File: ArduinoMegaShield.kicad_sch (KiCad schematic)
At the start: 23 parts, among them J1 Power, J10 Conn_01x04_Socket, J11 Conn_01x04_Socket, J2 PWM, J3 Analog, J4 PWM, J5 Analog, J6 Communication, J7 Digital, J8 Conn_01x04_Socket, J9 Conn_01x04_Socket, Q1 IRLB8721PBF, Q2 IRLB8721PBF, U1 MP6500_Pololu, U2 MP6500_Pololu

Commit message: Finished Schematic
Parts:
- removed J10, J11: Conn_01x04_Socket, symbol Connector:Conn_01x04_Socket
- removed R2, R3, R5, R6: 20R, symbol Device:R_US
- added J11, J12, J13, J14: Conn_01x02_Socket, Connector_PinSocket_2.54mm:PinSocket_1x02_P2.54mm_Vertical, symbol Connector:Conn_01x02_Socket
- added J15, J16: Conn_01x04, Connector_JST:JST_EH_S4B-EH_1x04_P2.50mm_Horizontal, symbol Connector_Generic:Conn_01x04
- added J17: Conn_01x10_Socket, Connector_PinSocket_2.54mm:PinSocket_1x10_P2.54mm_Vertical, symbol Connector:Conn_01x10_Socket
- added J18: Barrel_Jack_Switch, Connector_BarrelJack:BarrelJack_CUI_PJ-102AH_Horizontal, symbol Connector:Barrel_Jack_Switch
- added J9: Conn_01x04_Socket, Connector_PinSocket_2.54mm:PinSocket_1x04_P2.54mm_Vertical, symbol Connector:Conn_01x04_Socket
- added Q3, Q4, Q5, Q6, Q7: IRLB8721PBF, Package_TO_SOT_THT:TO-220-3_Vertical, symbol Transistor_FET:IRLB8721PBF
- added R2, R3, R5, R6, R7: 10K, Resistor_SMD:R_0805_2012Metric_Pad1.20x1.40mm_HandSolder, symbol Device:R
- C1, C2: footprint (none) -> Capacitor_THT:CP_Radial_D6.3mm_P2.50mm
- J10: renamed from J9; footprint (none) -> Connector_PinSocket_2.54mm:PinSocket_1x04_P2.54mm_Vertical
- J8: footprint (none) -> Connector_PinSocket_2.54mm:PinSocket_1x04_P2.54mm_Vertical
- R1, R4: footprint (none) -> Resistor_SMD:R_0805_2012Metric_Pad1.20x1.40mm_HandSolder
- U1, U2: footprint (none) -> Module:Pololu_Breakout-16_15.2x20.3mm
- renumbered J3 to J2, J5 to J3, J7 to J4, J2 to J5, J4 to J6, J6 to J7
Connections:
- net *10: now also Q7.1 (G), R7.1
- net *11: now also Q1.1 (G), R1.1
- net *12: now also Q2.1 (G), R2.1
- net *6: now also Q3.1 (G), R3.1
- net *7: now also R4.1, Q4.1 (G)
- net *8: now also Q5.1 (G), R5.1
- net *9: now also Q6.1 (G), R6.1
- net +12V: now also U1.16 (VMOT), U2.16 (VMOT), J11.1 (Pin_1), J11.2 (Pin_2), J13.1 (Pin_1), J13.2 (Pin_2), J17.1 (Pin_1), J17.3 (Pin_3), J17.5 (Pin_5), J17.7 (Pin_7), J17.9 (Pin_9), J18.1; no longer U1.9 (VMOT), U2.9 (VMOT)
- net GND: now also U1.15 (GND), U1.9 (GND), U2.15 (GND), U2.9 (GND), J18.2, J9.2 (Pin_2), Q3.3 (S), Q4.3 (S), Q5.3 (S), Q6.3 (S), Q7.3 (S), R2.2, R3.2, R5.2, R6.2, R7.2; no longer U1.10 (GND), U1.16 (GND), U2.10 (GND), U2.16 (GND)
- net SCL/21: now also J9.3 (Pin_3)
- net SDA/20: now also J9.4 (Pin_4)
- net VCC: now also J9.1 (Pin_1)
- net at U1.11 (A2): now also J15.4 (Pin_4)
- net at U1.12 (A1): now also J15.3 (Pin_3)
- net at U1.13 (B1): now also J15.2 (Pin_2)
- net at U1.14 (B2): now also J15.1 (Pin_1)
- net at Q1.2 (D): now also J12.1 (Pin_1), J12.2 (Pin_2)
- net at U2.11 (A2): now also J16.4 (Pin_4)
- net at U2.12 (A1): now also J16.3 (Pin_3)
- net at U2.13 (B1): now also J16.2 (Pin_2)
- net at U2.14 (B2): now also J16.1 (Pin_1)
- net at Q2.2 (D): now also J14.1 (Pin_1), J14.2 (Pin_2)
- new net: J17.10 (Pin_10), Q7.2 (D)
- new net: J17.2 (Pin_2), Q3.2 (D)
- new net: J17.4 (Pin_4), Q4.2 (D)
- new net: J17.6 (Pin_6), Q5.2 (D)
- new net: J17.8 (Pin_8), Q6.2 (D)
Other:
- note added: "Heating Capacitors (zigzag Resistors)"
- note added: "Heating Capacitors between"
- note added: "J15 and J16 CONNECTORS STILL UNDECIDED"
- note added: "Power Supply"
- note added: "Valve MOSFETs"
- title: (none) -> Arduino Mega Shield Schematic (Sylveon)
- moved on the sheet: J10, Q1, R1

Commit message: Update
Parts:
- J15, J16: footprint Connector_JST:JST_EH_S4B-EH_1x04_P2.50mm_Horizontal -> Connector_JST:JST_XH_B4B-XH-A_1x04_P2.50mm_Vertical
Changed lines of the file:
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@@
 			)
 		)
-		(property "Footprint" "Connector_JST:JST_EH_S4B-EH_1x04_P2.50mm_Horizontal"
+		(property "Footprint" "Connector_JST:JST_XH_B4B-XH-A_1x04_P2.50mm_Vertical"
 			(at 154.94 39.37 0)
 			(effects
@@
 			)
 		)
-		(property "Footprint" "Connector_JST:JST_EH_S4B-EH_1x04_P2.50mm_Horizontal"
+		(property "Footprint" "Connector_JST:JST_XH_B4B-XH-A_1x04_P2.50mm_Vertical"
 			(at 218.44 39.37 0)
 			(effects

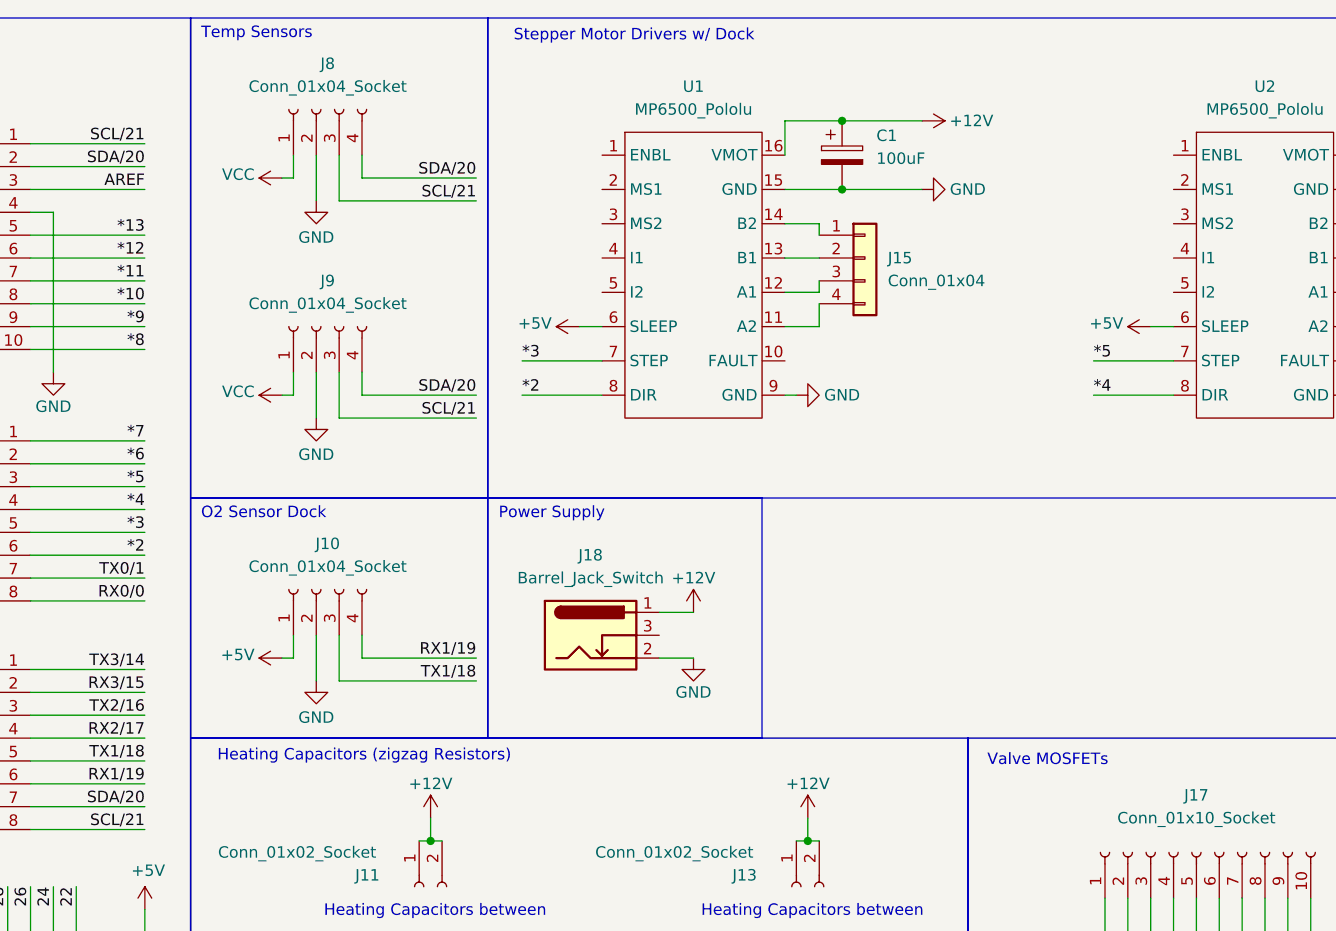
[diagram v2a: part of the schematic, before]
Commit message: Layout Placement done
-no fuse yet
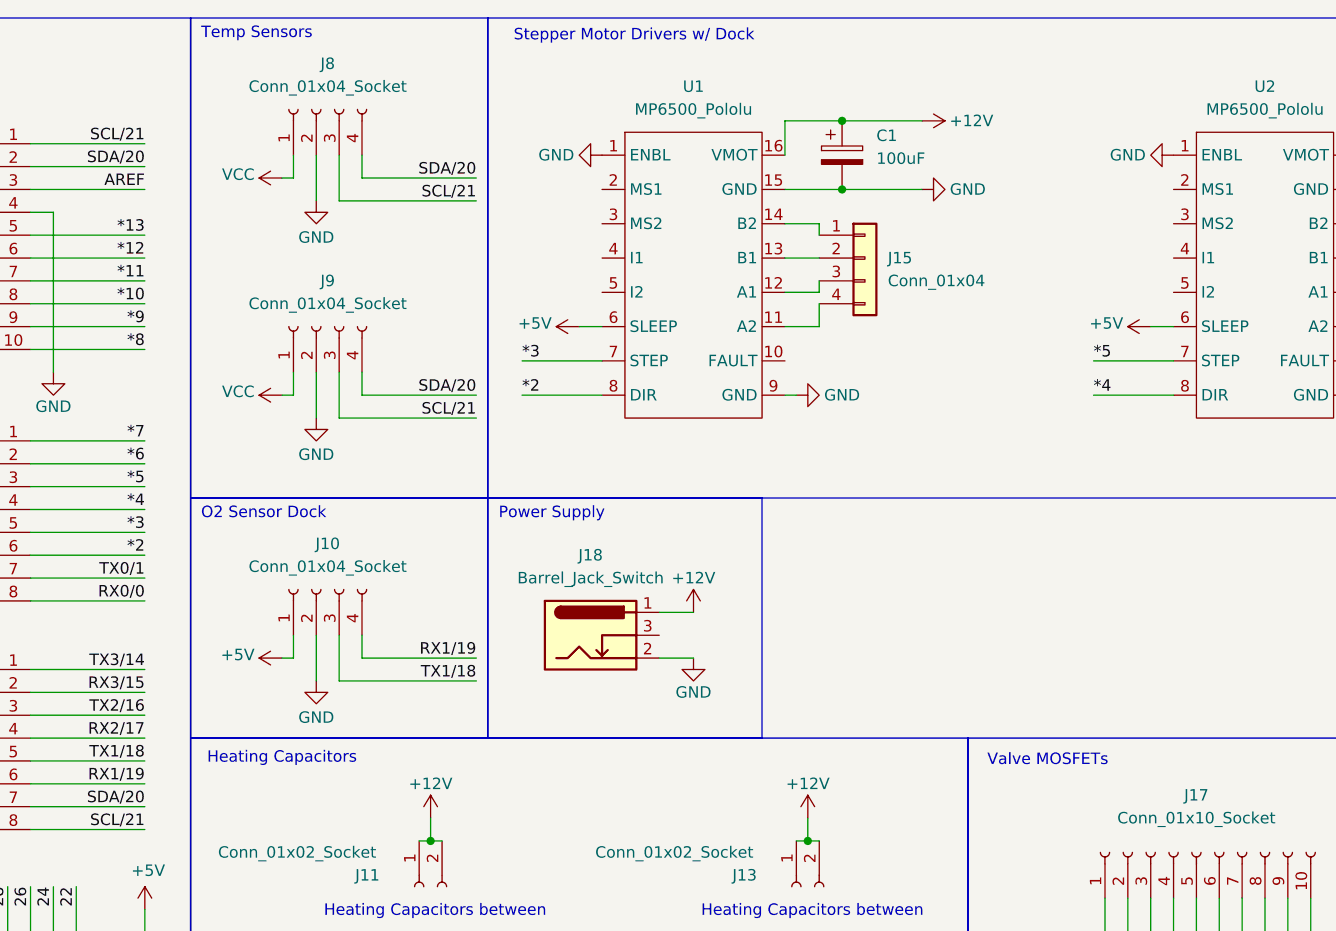
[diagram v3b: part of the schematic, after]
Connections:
- net GND: now also U1.1 (ENBL), U2.1 (ENBL)
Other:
- note added: "Heating Capacitors"
- note removed: "Heating Capacitors (zigzag Resistors)"
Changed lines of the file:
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@@
 		)
 	)
-	(text "Heating Capacitors (zigzag Resistors)"
+	(text "Heating Capacitors"
 		(exclude_from_sim no)
-		(at 99.314 94.742 0)
+		(at 90.17 94.996 0)
 		(effects
 			(font
@@
 	(symbol
 		(lib_id "power:GND")
+		(at 189.23 27.94 270)
+		(unit 1)
+		(exclude_from_sim no)
+		(in_bom yes)
+		(on_board yes)
+		(dnp no)
+		(property "Reference" "#PWR042"
+			(at 182.88 27.94 0)
+			(effects
+				(font
+					(size 1.27 1.27)
+				)
+				(hide yes)
+			)
+		)
+		(property "Value" "GND"
+			(at 184.15 27.94 90)
+			(effects
+				(font
+					(size 1.27 1.27)
+				)
+			)
+		)
+		(property "Footprint" ""
+			(at 189.23 27.94 0)
+			(effects
+				(font
+					(size 1.27 1.27)
+				)
+			)
+		)
+		(property "Datasheet" ""
+			(at 189.23 27.94 0)
+			(effects
+				(font
+					(size 1.27 1.27)
+				)
+			)
+		)
+		(property "Description" ""
+			(at 189.23 27.94 0)
+			(effects
+				(font
+					(size 1.27 1.27)
+				)
+				(hide yes)
+			)
+		)
+		(pin "1"
+		)
+		(instances
+			(project "ArduinoMegaShield"
+				(path "/e63e39d7-6ac0-4ffd-8aa3-1841a4541b55"
+					(reference "#PWR042")
+					(unit 1)
+				)
+			)
+		)
+	)
+	(symbol
+		(lib_id "power:GND")
 		(at 175.26 139.7 0)
 		(unit 1)
@@
 					(unit 1)
 				)
+			)
+		)
+	)
+	(symbol
+		(lib_id "power:GND")
+		(at 125.73 27.94 270)
+		(unit 1)
+		(exclude_from_sim no)
+		(in_bom yes)
+		(on_board yes)
+		(dnp no)
+		(property "Reference" "#PWR041"
+			(at 119.38 27.94 0)
+			(effects
+				(font
+					(size 1.27 1.27)
+				)
+				(hide yes)
+			)
+		)
+		(property "Value" "GND"
+			(at 120.65 27.94 90)
+			(effects
+				(font
+					(size 1.27 1.27)
+				)
+			)
+		)
+		(property "Footprint" ""
+			(at 125.73 27.94 0)
+			(effects
+				(font
+					(size 1.27 1.27)
+				)
+			)
+		)
+		(property "Datasheet" ""
+			(at 125.73 27.94 0)
+			(effects
+				(font
+					(size 1.27 1.27)
+				)
+			)
+		)
+		(property "Description" ""
+			(at 125.73 27.94 0)
+			(effects
+				(font
+					(size 1.27 1.27)
+				)
+				(hide yes)
+			)
+		)
+		(pin "1"
+		)
+		(instances
+			(project "ArduinoMegaShield"
+				(path "/e63e39d7-6ac0-4ffd-8aa3-1841a4541b55"
+					(reference "#PWR041")
+					(unit 1)
+				)

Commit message: Final Layout
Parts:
- removed J11, J12, J13, J14: Conn_01x02_Socket, Connector_PinSocket_2.54mm:PinSocket_1x02_P2.54mm_Vertical, symbol Connector:Conn_01x02_Socket
- removed J17: Conn_01x10_Socket, Connector_PinSocket_2.54mm:PinSocket_1x10_P2.54mm_Vertical, symbol Connector:Conn_01x10_Socket
- removed J18: Barrel_Jack_Switch, Connector_BarrelJack:BarrelJack_CUI_PJ-102AH_Horizontal, symbol Connector:Barrel_Jack_Switch
- added F1: Fuse, Fuse:Fuseholder_TR5_Littelfuse_No560_No460, symbol Device:Fuse
- added J11, J12: Conn_01x03_Socket, Connector_PinSocket_2.54mm:PinSocket_1x03_P2.54mm_Vertical, symbol Connector:Conn_01x03_Socket
- added J15, J16: Conn_01x05_Socket, Connector_PinSocket_2.54mm:PinSocket_1x05_P2.54mm_Vertical, symbol Connector:Conn_01x05_Socket
- added J17: L721RAHLP, L721RAHLP:SWITCHCRAFT_L721RAHLP, symbol L721RAHLP:L721RAHLP
- added SW1: 450301014042, footprints:SW_450301014042_WRE, symbol Switch:450301014042
- renumbered J15 to J13, J16 to J14
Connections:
- net +12V: now also F1.2, J11.2 (Pin_2), J11.3 (Pin_3), J12.2 (Pin_2), J12.3 (Pin_3), J16.1 (Pin_1), J16.2 (Pin_2), J16.3 (Pin_3), J16.4 (Pin_4), J16.5 (Pin_5), SW1.1
- net +5V: now also J8.1 (Pin_1), J9.1 (Pin_1)
- net GND: now also J17.S
- net VCC: now also SW1.2; no longer J8.1 (Pin_1), J9.1 (Pin_1)
- net at Q1.2 (D): now also J11.1 (Pin_1)
- net at Q7.2 (D): now also J15.5 (Pin_5)
- net at Q3.2 (D): now also J15.1 (Pin_1)
- net at Q4.2 (D): now also J15.2 (Pin_2)
- net at Q5.2 (D): now also J15.3 (Pin_3)
- net at Q6.2 (D): now also J15.4 (Pin_4)
- net at Q2.2 (D): now also J12.1 (Pin_1)
- new net: F1.1, J17.C
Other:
- note added: "Heating Capacitors between 1 and 2/3"
- note added: "Valves between"
- note removed: "Heating Capacitors between"
- note removed: "J15 and J16 CONNECTORS STILL UNDECIDED"
- moved on the sheet: Q1, Q2, R1, R2

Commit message: fixed for DRC
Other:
- note added: "Heating Elements"
- note added: "Heating Elements between 1 and 2/3"
- note removed: "Heating Capacitors"
- note removed: "Heating Capacitors between 1 and 2/3"
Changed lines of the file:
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@@
 		)
 	)
-	(text "Heating Capacitors\nbetween 1 and 2/3"
+	(text "Heating Elements\nbetween 1 and 2/3"
 		(exclude_from_sim no)
 		(at 91.186 113.03 0)
@@
 		)
 	)
-	(text "Heating Capacitors\nbetween 1 and 2/3"
+	(text "Heating Elements\nbetween 1 and 2/3"
 		(exclude_from_sim no)
 		(at 133.096 113.03 0)
@@
 		)
 	)
-	(text "Heating Capacitors"
+	(text "Heating Elements"
 		(exclude_from_sim no)
 		(at 90.17 94.996 0)
